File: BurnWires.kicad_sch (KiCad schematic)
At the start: 44 parts, among them Q10 IRLML2803, Q11 IRFTS9342PBF, Q5 MMBT2222AT, Q6 IRLML2803, Q7 IRFTS9342PBF, Q8 IRLML2803, Q9 IRFTS9342PBF, U2 PE014006

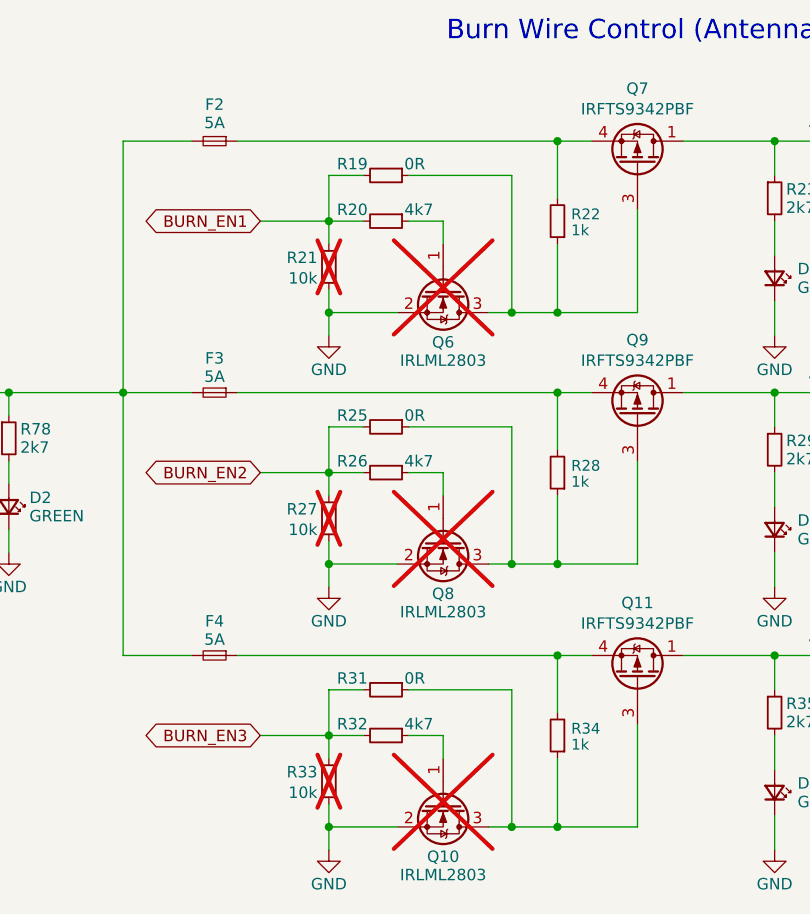
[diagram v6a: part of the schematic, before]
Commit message: Update DNP list
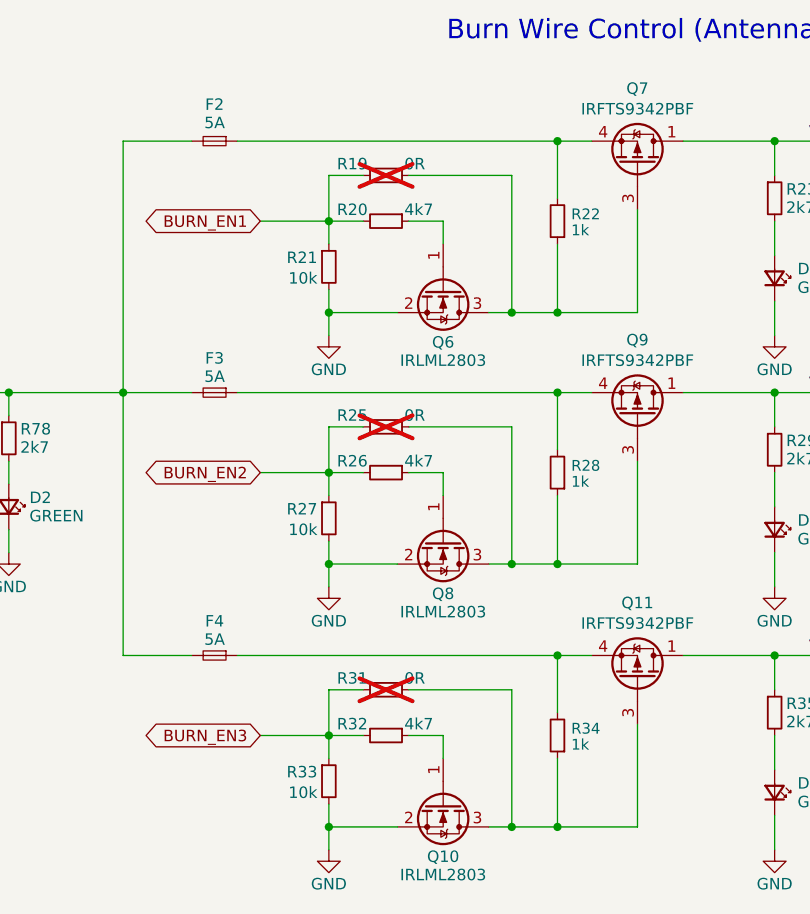
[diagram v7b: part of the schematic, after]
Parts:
- Q10, Q6, Q8, R21, R27, R33: now fitted; now in the parts list
- R19, R25, R31: now not fitted; now left out of the parts list
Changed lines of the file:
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@@
 		(unit 1)
 		(exclude_from_sim no)
-		(in_bom no)
+		(in_bom yes)
 		(on_board yes)
-		(dnp yes)
+		(dnp no)
 		(property "Reference" "R27"
 			(at 160.02 104.394 0)
@@
 		(unit 1)
 		(exclude_from_sim no)
-		(in_bom yes)
+		(in_bom no)
 		(on_board yes)
-		(dnp no)
+		(dnp yes)
 		(property "Reference" "R19"
 			(at 165.608 66.04 90)
@@
 		(unit 1)
 		(exclude_from_sim no)
-		(in_bom no)
+		(in_bom yes)
 		(on_board yes)
-		(dnp yes)
+		(dnp no)
 		(property "Reference" "Q8"
 			(at 173.99 113.792 90)
@@
 		(unit 1)
 		(exclude_from_sim no)
-		(in_bom yes)
+		(in_bom no)
 		(on_board yes)
-		(dnp no)
+		(dnp yes)
 		(property "Reference" "R31"
 			(at 165.608 123.19 90)
@@
 		(unit 1)
 		(exclude_from_sim no)
-		(in_bom no)
+		(in_bom yes)
 		(on_board yes)
-		(dnp yes)
+		(dnp no)
 		(property "Reference" "R33"
 			(at 160.02 133.604 0)
@@
 		(unit 1)
 		(exclude_from_sim no)
-		(in_bom no)
+		(in_bom yes)
 		(on_board yes)
-		(dnp yes)
+		(dnp no)
 		(property "Reference" "R21"
 			(at 160.02 76.454 0)
@@
 		(unit 1)
 		(exclude_from_sim no)
-		(in_bom no)
+		(in_bom yes)
 		(on_board yes)
-		(dnp yes)
+		(dnp no)
 		(property "Reference" "Q6"
 			(at 173.99 85.852 90)
@@
 		(unit 1)
 		(exclude_from_sim no)
-		(in_bom yes)
+		(in_bom no)
 		(on_board yes)
-		(dnp no)
+		(dnp yes)
 		(property "Reference" "R25"
 			(at 165.608 93.98 90)
@@
 		(unit 1)
 		(exclude_from_sim no)
-		(in_bom no)
+		(in_bom yes)
 		(on_board yes)
-		(dnp yes)
+		(dnp no)
 		(property "Reference" "Q10"
 			(at 173.99 143.002 90)
